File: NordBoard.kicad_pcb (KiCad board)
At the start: 2 copper layers, 271.2 x 89.5 mm, 94 parts, among them P1 USB_C_Plug_USB2.0, P2 USB_C_Plug_USB2.0, SW1 SW_Push, SW10 SW_Push, SW11 SW_Push, SW12 SW_Push, SW13 SW_Push, SW14 SW_Push, SW15 SW_Push, SW16 SW_Push, SW17 SW_Push, SW18 SW_Push, SW19 SW_Push, SW2 SW_Push, SW20 SW_Push, SW21 SW_Push, SW22 SW_Push, SW23 SW_Push, SW24 SW_Push, SW25 SW_Push, SW26 SW_Push, SW27 SW_Push, SW28 SW_Push, SW29 SW_Push, SW3 SW_Push, SW30 SW_Push, SW31 SW_Push, SW32 SW_Push, SW33 SW_Push, SW34 SW_Push, SW35 SW_Push, SW36 SW_Push, SW37 SW_Push, SW38 SW_Push, SW39 SW_Push, SW4 SW_Push, SW40 SW_Push, SW5 SW_Push, SW50 SW_Push, SW51 SW_Push, SW6 SW_Push, SW7 SW_Push, SW8 SW_Push, SW9 SW_Push, U1 XIAO-RP2040-DIP, U2 XIAO-RP2040-DIP

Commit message: chore: sync before reroute
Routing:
- net /GND_R: track 11.6 -> 22.8 mm, vias 0 -> 1
- net /GND_L: track 12.4 -> 23.3 mm, vias 0 -> 1
- net /COL8: track 120.2 -> 114.3 mm
- net /COL11: track 194.8 -> 200.6 mm
- net /COL7: track 100.0 -> 95.7 mm
- net /COL6: track 74.4 -> 73.8 mm

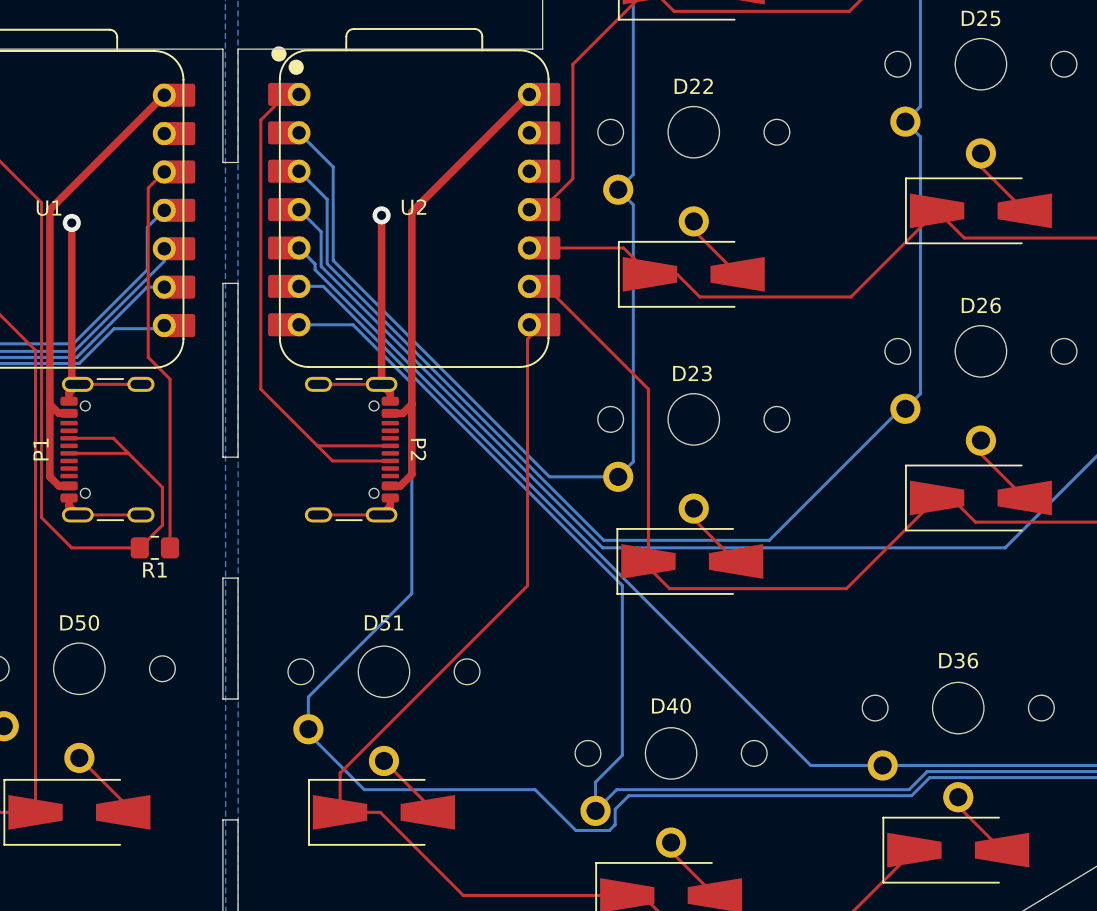
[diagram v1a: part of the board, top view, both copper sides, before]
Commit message: feat: improve traces, add jlcpcb export, new journal
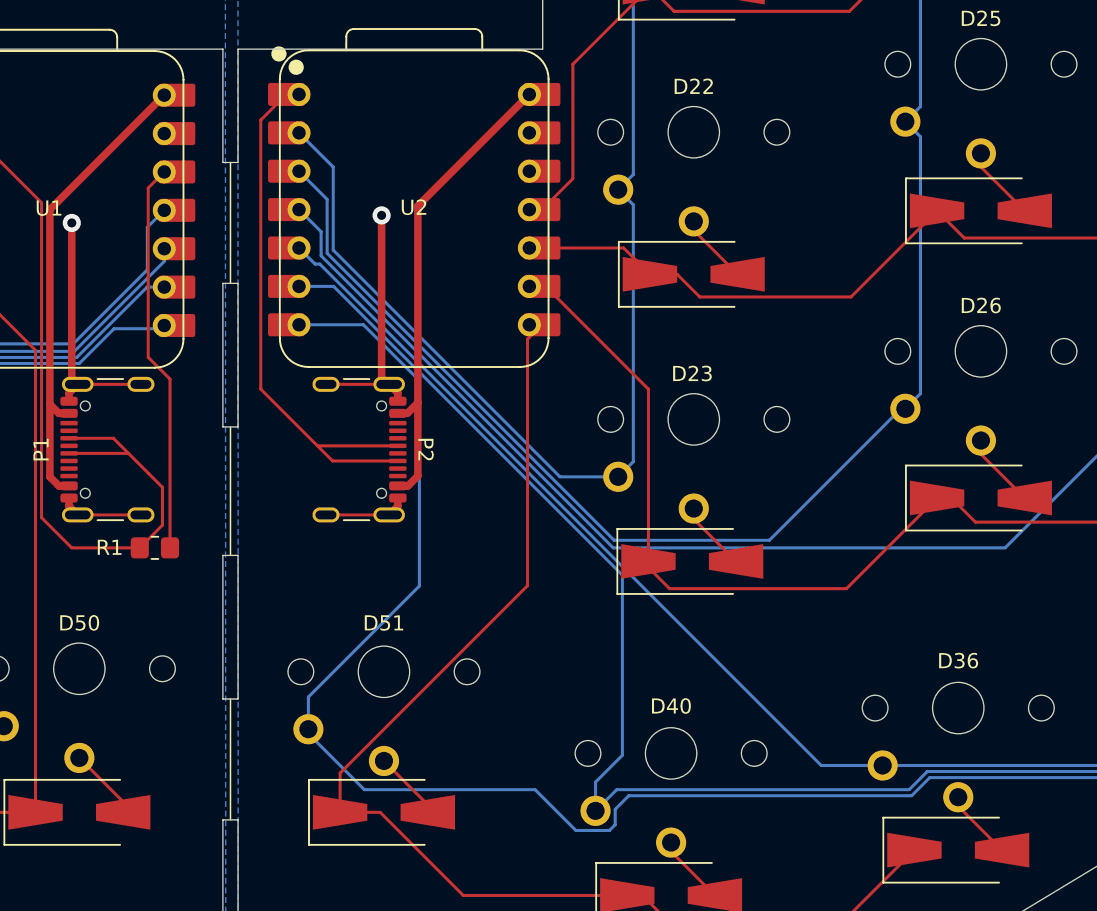
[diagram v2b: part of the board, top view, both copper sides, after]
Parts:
- moved P2 0.50 mm to (154.9, 115.5)
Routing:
- net /INTERCON_R: track 35.6 -> 36.6 mm
- net /COL11: track 200.6 -> 201.4 mm
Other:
- outline, holes or cut-outs redrawn
